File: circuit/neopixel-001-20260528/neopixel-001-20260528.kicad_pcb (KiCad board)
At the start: 2 copper layers, 114.3 x 114.3 mm, 0 parts

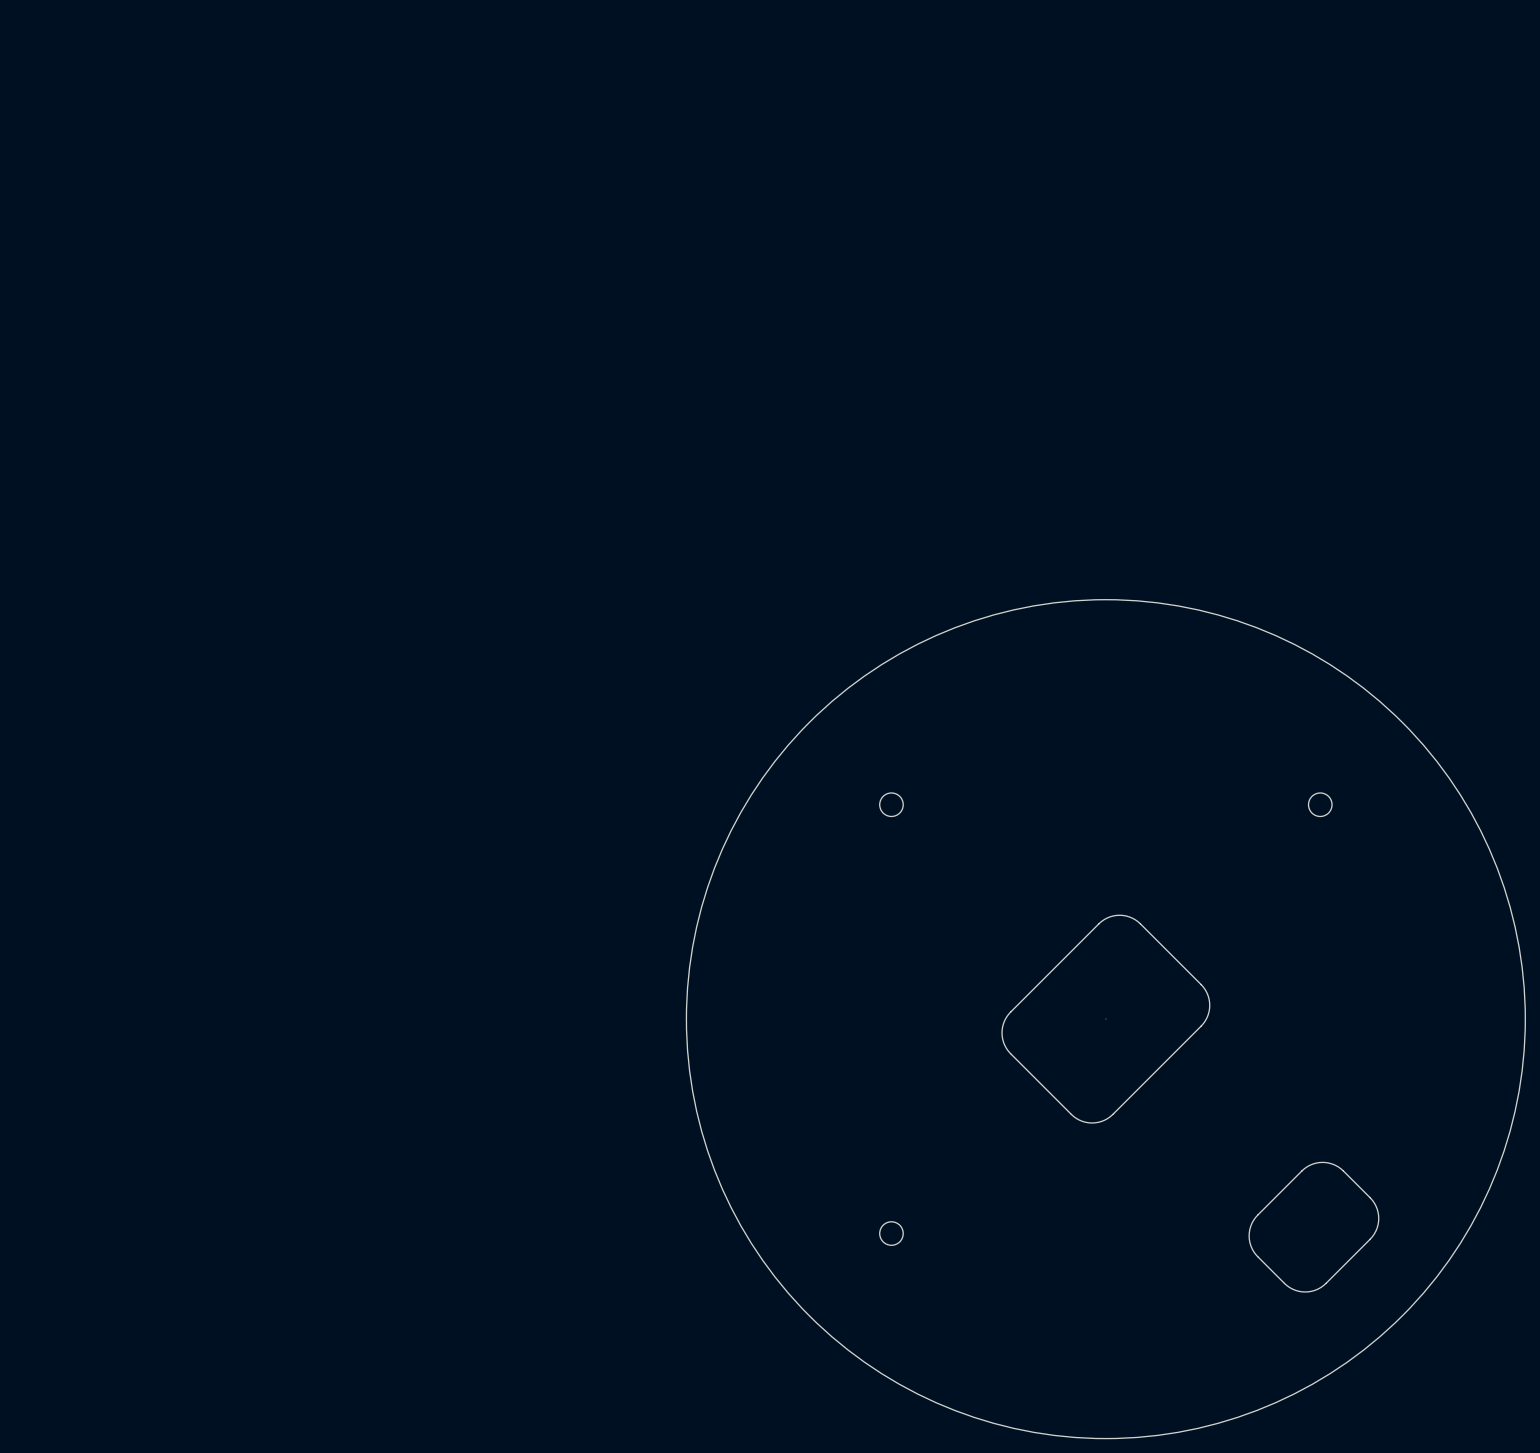
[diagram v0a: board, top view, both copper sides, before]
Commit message: Update NeoPixel基板の部品配置を開始
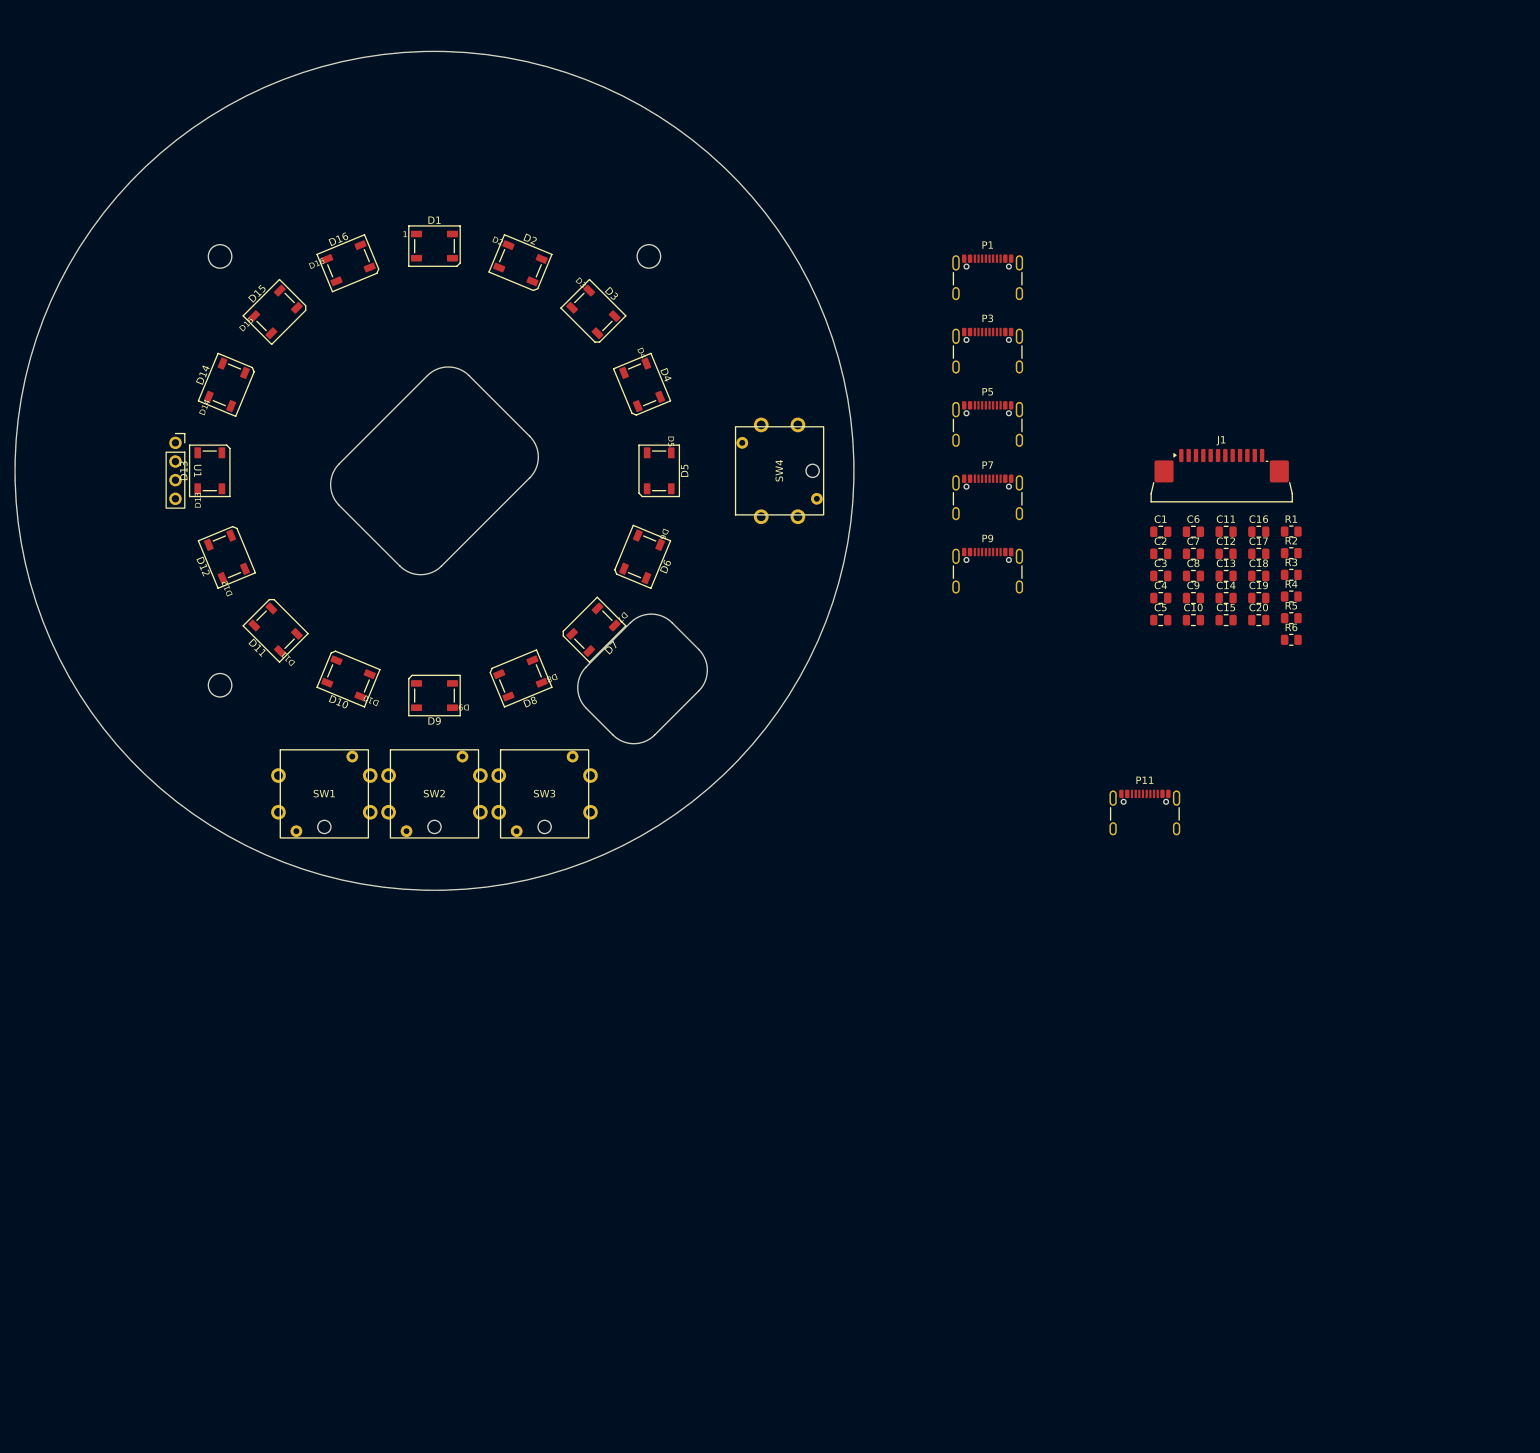
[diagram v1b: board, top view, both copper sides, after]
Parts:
- added C1: 100n, Capacitor_SMD:C_0805_2012Metric, F.Cu at (98.9, 8.29)
- added C10: 100n, Capacitor_SMD:C_0805_2012Metric, F.Cu at (103.4, 20.3)
- added C11: 100n, Capacitor_SMD:C_0805_2012Metric, F.Cu at (107.8, 8.29)
- added C12: 100n, Capacitor_SMD:C_0805_2012Metric, F.Cu at (107.8, 11.3)
- added C13: 100n, Capacitor_SMD:C_0805_2012Metric, F.Cu at (107.8, 14.3)
- added C14: 100n, Capacitor_SMD:C_0805_2012Metric, F.Cu at (107.8, 17.3)
- added C15: 100n, Capacitor_SMD:C_0805_2012Metric, F.Cu at (107.8, 20.3)
- added C16: 100n, Capacitor_SMD:C_0805_2012Metric, F.Cu at (112.3, 8.29)
- added C17: 100n, Capacitor_SMD:C_0805_2012Metric, F.Cu at (112.3, 11.3)
- added C18: 100n, Capacitor_SMD:C_0805_2012Metric, F.Cu at (112.3, 14.3)
- added C19: 100n, Capacitor_SMD:C_0805_2012Metric, F.Cu at (112.3, 17.3)
- added C2: 100n, Capacitor_SMD:C_0805_2012Metric, F.Cu at (98.9, 11.3)
- added C20: 100n, Capacitor_SMD:C_0805_2012Metric, F.Cu at (112.3, 20.3)
- added C3: 100n, Capacitor_SMD:C_0805_2012Metric, F.Cu at (98.9, 14.3)
- added C4: 100n, Capacitor_SMD:C_0805_2012Metric, F.Cu at (98.9, 17.3)
- added C5: 100n, Capacitor_SMD:C_0805_2012Metric, F.Cu at (98.9, 20.3)
- added C6: 100n, Capacitor_SMD:C_0805_2012Metric, F.Cu at (103.4, 8.29)
- added C7: 100n, Capacitor_SMD:C_0805_2012Metric, F.Cu at (103.4, 11.3)
- added C8: 100n, Capacitor_SMD:C_0805_2012Metric, F.Cu at (103.4, 14.3)
- added C9: 100n, Capacitor_SMD:C_0805_2012Metric, F.Cu at (103.4, 17.3)
- added D1: WS2812B, LED_SMD:LED_WS2812B_PLCC4_5.0x5.0mm_P3.2mm, F.Cu at (0.00, -30.6)
- added D10: WS2812B, LED_SMD:LED_WS2812B_PLCC4_5.0x5.0mm_P3.2mm, F.Cu at (-11.7, 28.3)
- added D11: WS2812B, LED_SMD:LED_WS2812B_PLCC4_5.0x5.0mm_P3.2mm, F.Cu at (-21.6, 21.6)
- added D12: WS2812B, LED_SMD:LED_WS2812B_PLCC4_5.0x5.0mm_P3.2mm, F.Cu at (-28.3, 11.7)
- added D13: WS2812B, LED_SMD:LED_WS2812B_PLCC4_5.0x5.0mm_P3.2mm, F.Cu at (-30.6, 0.00)
- added D14: WS2812B, LED_SMD:LED_WS2812B_PLCC4_5.0x5.0mm_P3.2mm, F.Cu at (-28.3, -11.7)
- added D15: WS2812B, LED_SMD:LED_WS2812B_PLCC4_5.0x5.0mm_P3.2mm, F.Cu at (-21.6, -21.6)
- added D16: WS2812B, LED_SMD:LED_WS2812B_PLCC4_5.0x5.0mm_P3.2mm, F.Cu at (-11.7, -28.3)
- added D2: WS2812B, LED_SMD:LED_WS2812B_PLCC4_5.0x5.0mm_P3.2mm, F.Cu at (11.7, -28.3)
- added D3: WS2812B, LED_SMD:LED_WS2812B_PLCC4_5.0x5.0mm_P3.2mm, F.Cu at (21.6, -21.6)
- added D4: WS2812B, LED_SMD:LED_WS2812B_PLCC4_5.0x5.0mm_P3.2mm, F.Cu at (28.3, -11.7)
- added D5: WS2812B, LED_SMD:LED_WS2812B_PLCC4_5.0x5.0mm_P3.2mm, F.Cu at (30.6, 0.00)
- added D6: WS2812B, LED_SMD:LED_WS2812B_PLCC4_5.0x5.0mm_P3.2mm, F.Cu at (28.3, 11.7)
- added D7: WS2812B, LED_SMD:LED_WS2812B_PLCC4_5.0x5.0mm_P3.2mm, F.Cu at (21.6, 21.6)
- added D8: WS2812B, LED_SMD:LED_WS2812B_PLCC4_5.0x5.0mm_P3.2mm, F.Cu at (11.7, 28.3)
- added D9: WS2812B, LED_SMD:LED_WS2812B_PLCC4_5.0x5.0mm_P3.2mm, F.Cu at (0.00, 30.6)
- added J1: Conn_NeoPixel, Connector_FFC-FPC:JUSHUO_AFA07-S12FCA-00_1x12-1MP_P1.0mm_Horizontal, F.Cu at (107.2, 1.28)
- added P1: ESP32C3_{1}, Connector_USB:USB_C_Receptacle_GCT_USB4105-xx-A_16P_TopMnt_Horizontal, F.Cu at (75.3, -25.2)
- added P11: unitV4, Connector_USB:USB_C_Receptacle_GCT_USB4105-xx-A_16P_TopMnt_Horizontal, F.Cu at (96.8, 47.7)
- added P3: ESP32C3_{2}, Connector_USB:USB_C_Receptacle_GCT_USB4105-xx-A_16P_TopMnt_Horizontal, F.Cu at (75.3, -15.2)
- added P5: unitV1, Connector_USB:USB_C_Receptacle_GCT_USB4105-xx-A_16P_TopMnt_Horizontal, F.Cu at (75.3, -5.24)
- added P7: unitV2, Connector_USB:USB_C_Receptacle_GCT_USB4105-xx-A_16P_TopMnt_Horizontal, F.Cu at (75.3, 4.75)
- added P9: unitV3, Connector_USB:USB_C_Receptacle_GCT_USB4105-xx-A_16P_TopMnt_Horizontal, F.Cu at (75.3, 14.7)
- added R1: 1k, Resistor_SMD:R_0805_2012Metric, F.Cu at (116.7, 8.27)
- added R2: 1k, Resistor_SMD:R_0805_2012Metric, F.Cu at (116.7, 11.2)
- added R3: 10k, Resistor_SMD:R_0805_2012Metric, F.Cu at (116.7, 14.2)
- added R4: 10k, Resistor_SMD:R_0805_2012Metric, F.Cu at (116.7, 17.1)
- added R5: 10k, Resistor_SMD:R_0805_2012Metric, F.Cu at (116.7, 20.1)
- added R6: 10k, Resistor_SMD:R_0805_2012Metric, F.Cu at (116.7, 23.0)
- added SW1: SW_SPST, @Thrive_footprint_neopixel:ST-12-401FC-G, F.Cu at (-15.0, 44.0)
- added SW2: SW_SPST, @Thrive_footprint_neopixel:ST-12-401FC-G, F.Cu at (0.00, 44.0)
- added SW3: SW_SPST, @Thrive_footprint_neopixel:ST-12-401FC-G, F.Cu at (15.0, 44.0)
- added SW4: SW_SPST, @Thrive_footprint_neopixel:ST-12-401FC-G, F.Cu at (47.0, 0.00)
- added U1: SSD1306, @Thrive_footprint_neopixel:SSD1306_display_module, F.Cu at (-35.3, 0.00)
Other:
- outline, holes or cut-outs redrawn

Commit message: Update ネオピク基板の横向きUSBを配置
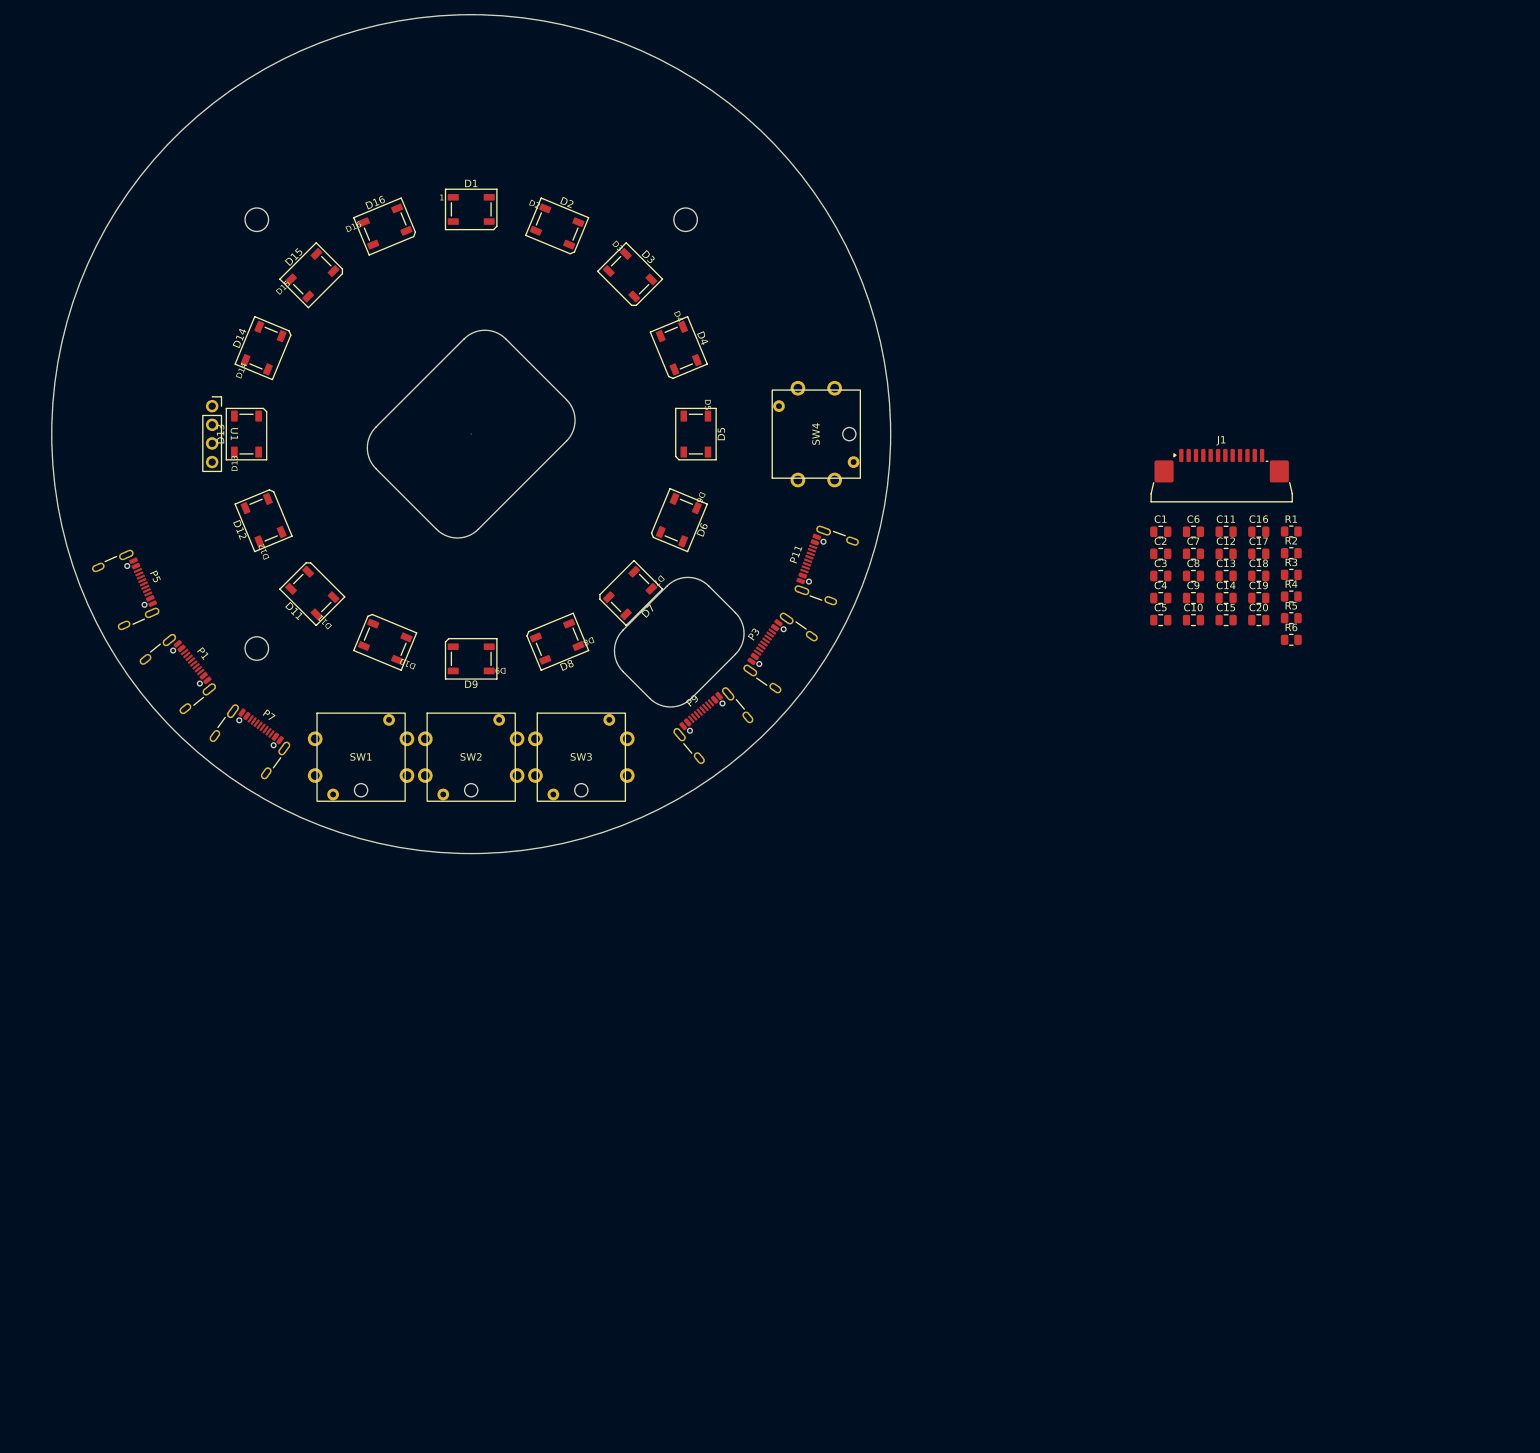
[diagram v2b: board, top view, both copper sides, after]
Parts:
- moved P1 123.4 mm to (-35.8, 28.4), turned to -51 degrees
- moved P5 120.4 mm to (-43.0, 16.7), turned to -66 degrees
- moved P7 106.4 mm to (-25.8, 37.8), turned to -36 degrees
- moved P11 54.5 mm to (54.4, 13.3), turned to 70 degrees
- moved P3 49.0 mm to (48.0, 25.4), turned to 55 degrees
- moved P9 42.1 mm to (38.7, 35.5), turned to 40 degrees
- moved D14 7.07 mm to (-23.3, -16.7)
- moved D2 7.07 mm to (16.7, -33.3)
- moved D4 7.07 mm to (33.3, -16.7)
- moved D8 7.07 mm to (16.7, 23.3)
- moved D11 7.07 mm to (-16.6, 16.6)
- moved D13 7.07 mm to (-25.6, -5.00)
- moved D15 7.07 mm to (-16.6, -26.6)
- moved D3 7.07 mm to (26.6, -26.6)
- moved D7 7.07 mm to (26.6, 16.6)
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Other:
- outline, holes or cut-outs redrawn

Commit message: Update NeoPixel基板のPCBをちょっとだけ触った
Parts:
- moved C13 7.07 mm to (102.8, 19.3)
- moved C18 7.07 mm to (107.3, 19.3)
- moved C3 7.07 mm to (93.9, 19.3)
- moved C8 7.07 mm to (98.4, 19.3)
- moved D14 7.07 mm to (-28.3, -11.7)
- moved D2 7.07 mm to (11.7, -28.3)
- moved D4 7.07 mm to (28.3, -11.7)
- moved D8 7.07 mm to (11.7, 28.3)
- moved P11 7.07 mm to (49.4, 18.3)
- moved C1 7.07 mm to (93.9, 13.3)
- moved C10 7.07 mm to (98.4, 25.3)
- moved C11 7.07 mm to (102.8, 13.3)
- moved C12 7.07 mm to (102.8, 16.3)
- moved C14 7.07 mm to (102.8, 22.3)
- moved C15 7.07 mm to (102.8, 25.3)
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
